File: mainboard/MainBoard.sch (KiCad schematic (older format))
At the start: 51 parts, among them J1 isoSPI, J11 Conn_01x02, J2 SWDebug, J3 IMD, J4 IO, U1 LTC6820, U10 REF2920, U2 HM2103, U3 M24M02, U4 M24M02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

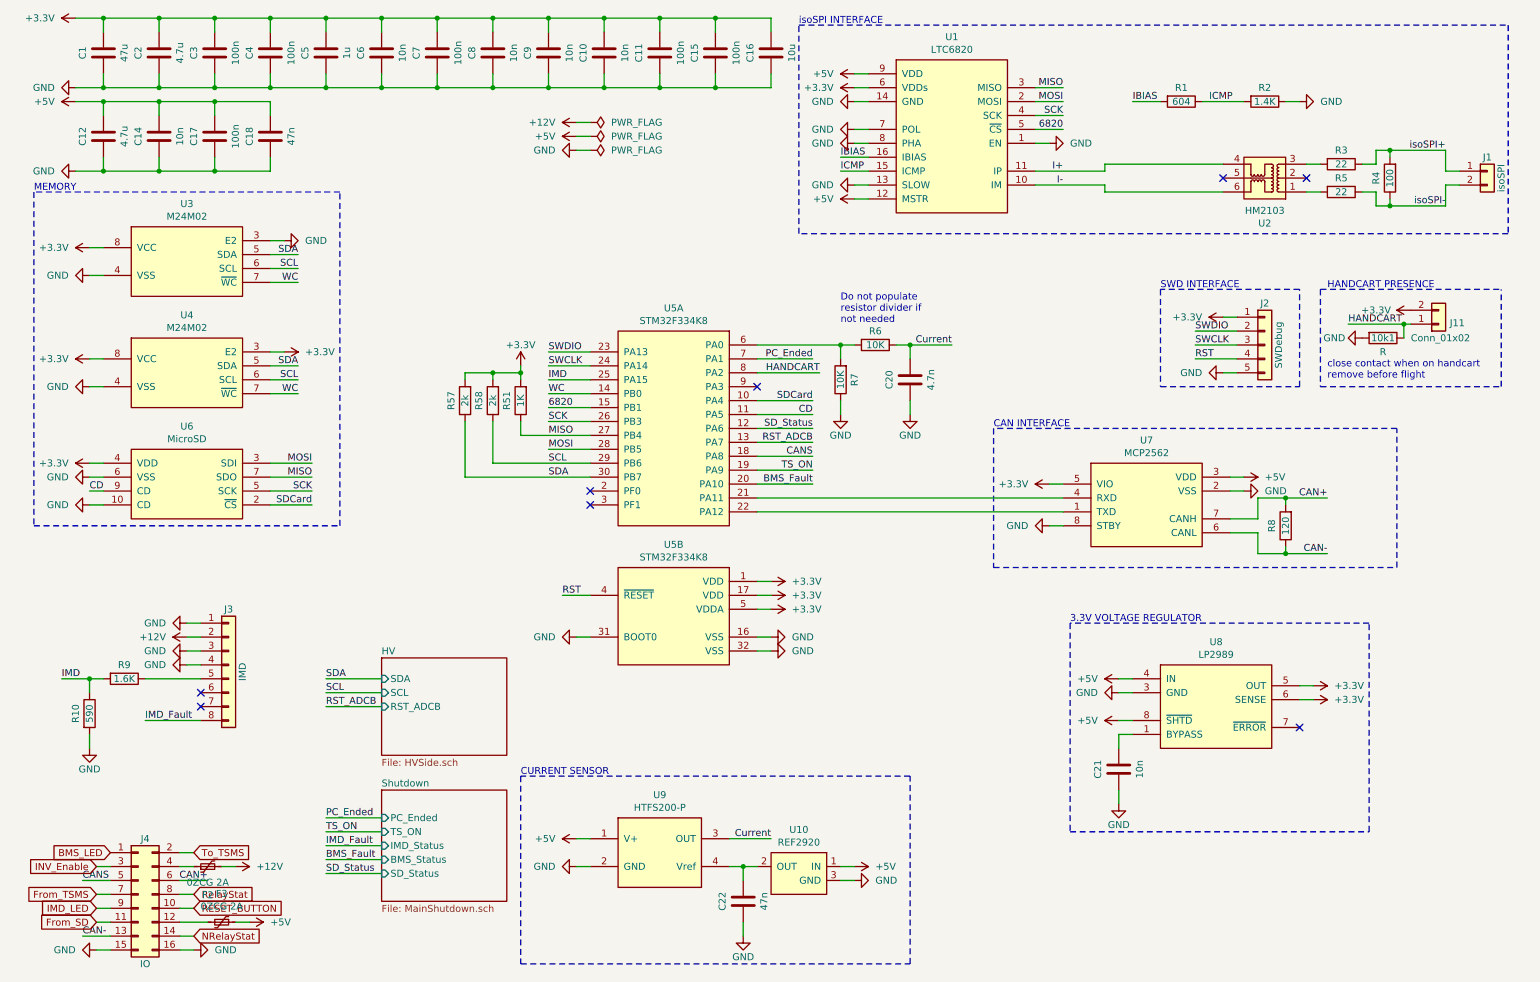
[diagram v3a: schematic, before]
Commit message: Shutdown logic to use gates, changed mosfets
Shutdown ported from new car, mosfets changed to higher VGS max
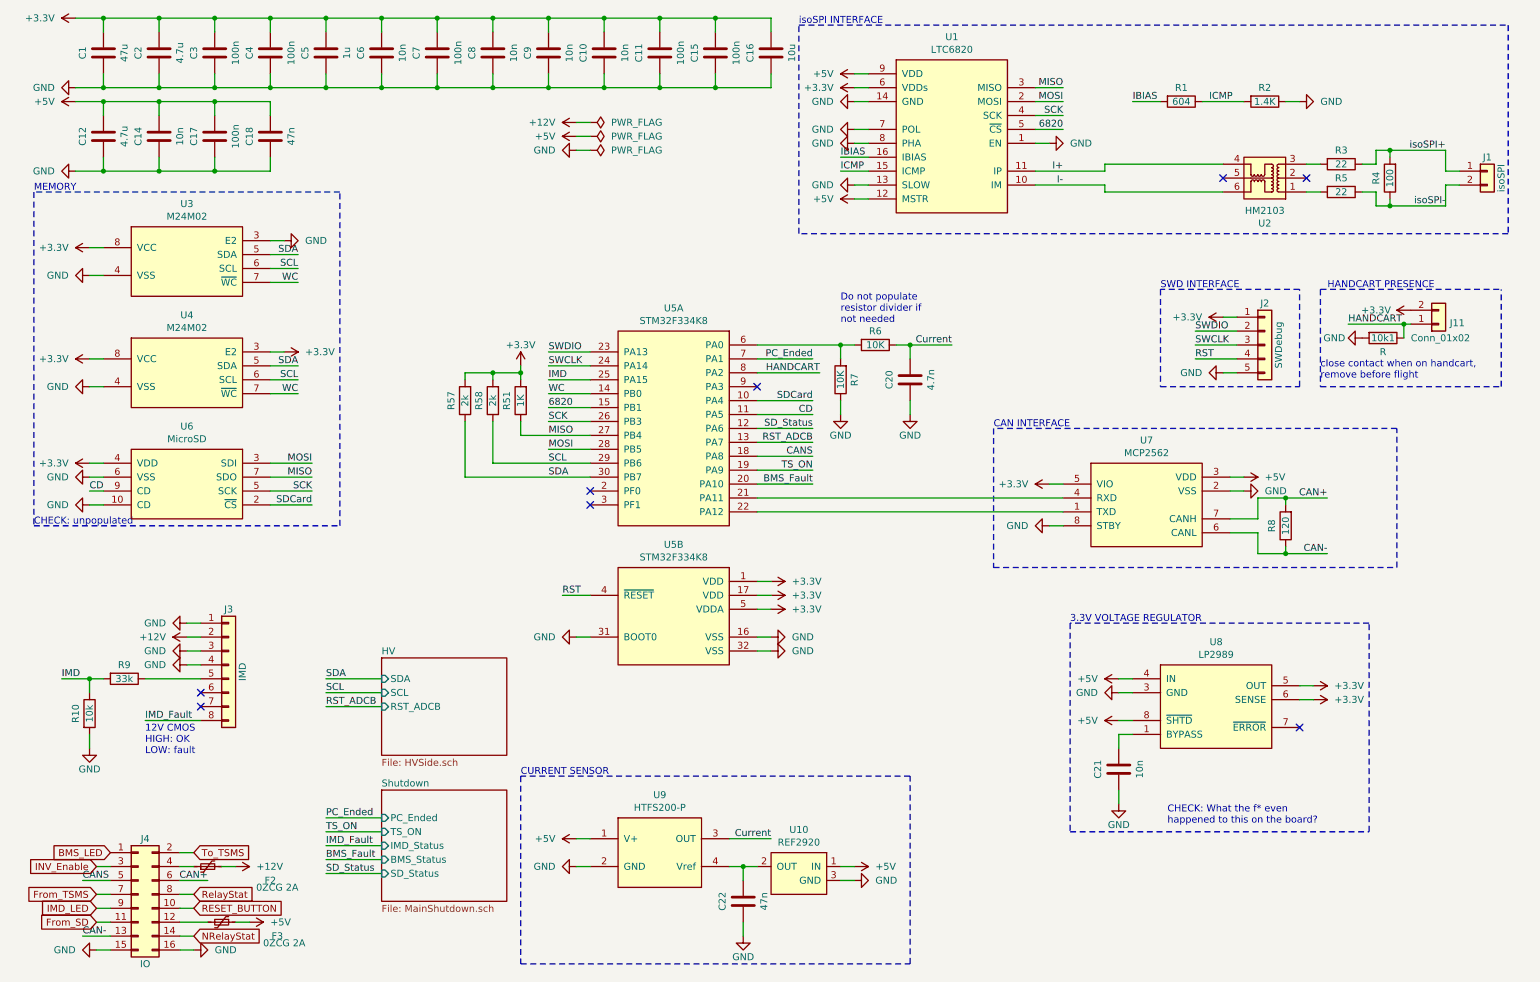
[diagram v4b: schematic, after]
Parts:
- R10: value 590 -> 10k
- R9: value 1.6K -> 33k
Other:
- note added: "12V CMOS\nHIGH: OK\nLOW: fault"
- note added: "CHECK: What the f* even \nhappened to this on the board?"
- note added: "CHECK: unpopulated"
- note added: "close contact when on handcart,\nremove before flight"
- note removed: "close contact when on handcart\nremove before flight"
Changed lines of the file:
@@
 Title ""
 Date ""
-Rev ""
+Rev "V3"
 Comp ""
 Comment1 ""
@@
 P 1000 5550
 F 0 "R10" V 900 5550 50  0000 C CNN
-F 1 "590" V 1000 5550 50  0000 C CNN
+F 1 "10k" V 1000 5550 50  0000 C CNN
 F 2 "Resistor_SMD:R_0805_2012Metric" V 930 5550 50  0001 C CNN
 F 3 "~" H 1000 5550 50  0001 C CNN
@@
 P 1250 5300
 F 0 "R9" V 1150 5300 50  0000 C CNN
-F 1 "1.6K" V 1250 5300 50  0000 C CNN
+F 1 "33k" V 1250 5300 50  0000 C CNN
 F 2 "Resistor_SMD:R_0805_2012Metric" V 1180 5300 50  0001 C CNN
 F 3 "~" H 1250 5300 50  0001 C CNN
@@
 U 1 1 5B2F3DA2
 P 1850 6650
-F 0 "F2" V 1645 6650 50  0000 C CNN
-F 1 "0ZCG 2A" V 1736 6650 50  0000 C CNN
+F 0 "F2" V 1750 6200 50  0000 C CNN
+F 1 "0ZCG 2A" V 1700 6150 50  0000 C CNN
 F 2 "Fuse:Fuse_1812_4532Metric" H 1900 6450 50  0001 L CNN
 F 3 "~" H 1850 6650 50  0001 C CNN
@@
 U 1 1 5B3092A1
 P 1950 7050
-F 0 "F3" V 1745 7050 50  0000 C CNN
-F 1 "0ZCG 2A" V 1836 7050 50  0000 C CNN
+F 0 "F3" V 2050 7450 50  0000 C CNN
+F 1 "0ZCG 2A" V 2100 7500 50  0000 C CNN
 F 2 "Fuse:Fuse_1812_4532Metric" H 2000 6850 50  0001 L CNN
 F 3 "~" H 1950 7050 50  0001 C CNN
@@
 Text Notes 9900 2500 0    50   ~ 0
 HANDCART PRESENCE
-Text Notes 9900 3150 0    50   ~ 0
-close contact when on handcart\nremove before flight
+Text Notes 9850 3150 0    50   ~ 0
+close contact when on handcart,\nremove before flight
 Wire Notes Line
 	9850 2500 9850 3200
@@
 	9850 3200 11150 3200
 NoConn ~ 5800 3200
+Text Notes 1400 5850 0    50   ~ 0
+12V CMOS\nHIGH: OK\nLOW: fault
+Text Notes 600  4200 0    50   ~ 0
+CHECK: unpopulated
+Text Notes 8750 6350 0    50   ~ 0
+CHECK: What the f* even \nhappened to this on the board?
 $EndSCHEMATC

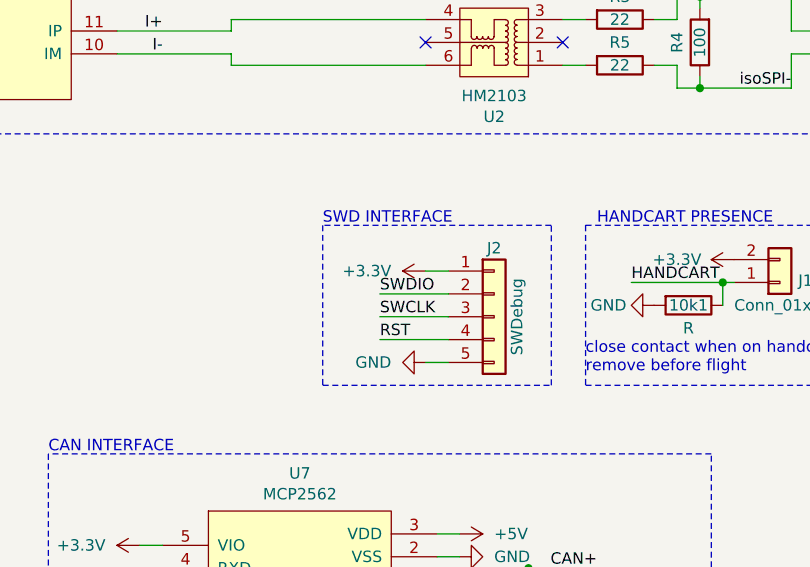
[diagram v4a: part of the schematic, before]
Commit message: new SWD connector
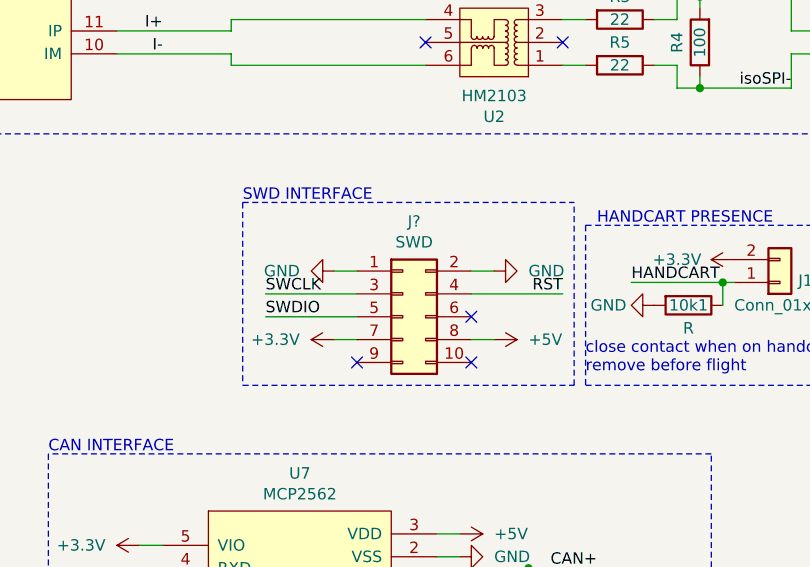
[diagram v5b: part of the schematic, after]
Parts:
- removed J2: SWDebug, Connector_PinHeader_2.54mm:PinHeader_1x05_P2.54mm_Vertical, symbol Connector_Generic:Conn_01x05
- added J?: SWD, symbol Connector_Generic:Conn_02x05_Odd_Even
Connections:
- net +3V3: now also J?.7 (Pin_7)
- net +5V: now also J?.8 (Pin_8)
- net GND: now also J?.1 (Pin_1), J?.2 (Pin_2)
- net RST: now also J?.4 (Pin_4)
- net SWCLK: now also J?.3 (Pin_3)
- net SWDIO: now also J?.5 (Pin_5)
- no-connect marks 8 -> 11
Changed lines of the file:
@@
 Text Label 4400 4700 0    50   ~ 0
 RST
-$Comp
-L Connector_Generic:Conn_01x05 J2
-U 1 1 5B04F48B
-P 9450 2900
-F 0 "J2" H 9450 3200 50  0000 C CNN
-F 1 "SWDebug" V 9550 2900 50  0000 C CNN
-F 2 "Connector_PinHeader_2.54mm:PinHeader_1x05_P2.54mm_Vertical" H 9450 2900 50  0001 C CNN
-F 3 "~" H 9450 2900 50  0001 C CNN
-	1    9450 2900
-	1    0    0    -1
-$EndComp
-Wire Wire Line
-	9250 2700 9150 2700
+Wire Wire Line
+	8850 3000 8750 3000
 $Comp
 L power:+3.3V #PWR021
 U 1 1 5B059441
-P 9150 2700
-F 0 "#PWR021" H 9150 2550 50  0001 C CNN
-F 1 "+3.3V" V 9150 2850 50  0000 L CNN
-F 2 "" H 9150 2700 50  0001 C CNN
-F 3 "" H 9150 2700 50  0001 C CNN
-	1    9150 2700
+P 8750 3000
+F 0 "#PWR021" H 8750 2850 50  0001 C CNN
+F 1 "+3.3V" V 8750 3150 50  0000 L CNN
+F 2 "" H 8750 3000 50  0001 C CNN
+F 3 "" H 8750 3000 50  0001 C CNN
+	1    8750 3000
 	0    -1   -1   0
 $EndComp
 Wire Wire Line
-	9250 3100 9150 3100
+	8850 2700 8750 2700
 $Comp
 L power:GND #PWR024
 U 1 1 5B0816C3
-P 9150 3100
-F 0 "#PWR024" H 9150 2850 50  0001 C CNN
-F 1 "GND" V 9150 2950 50  0000 R CNN
-F 2 "" H 9150 3100 50  0001 C CNN
-F 3 "" H 9150 3100 50  0001 C CNN
-	1    9150 3100
-	0    1    1    0
-$EndComp
-Text Label 8950 2800 0    50   ~ 0
+P 8750 2700
+F 0 "#PWR024" H 8750 2450 50  0001 C CNN
+F 1 "GND" V 8750 2550 50  0000 R CNN
+F 2 "" H 8750 2700 50  0001 C CNN
+F 3 "" H 8750 2700 50  0001 C CNN
+	1    8750 2700
+	0    1    1    0
+$EndComp
+Text Label 8450 2900 0    50   ~ 0
 SWDIO
-Text Label 8950 2900 0    50   ~ 0
+Text Label 8450 2800 0    50   ~ 0
 SWCLK
-Text Label 8950 3000 0    50   ~ 0
+Text Label 9750 2800 2    50   ~ 0
 RST
-Wire Wire Line
-	8950 2800 9250 2800
-Wire Wire Line
-	8950 2900 9250 2900
-Wire Wire Line
-	8950 3000 9250 3000
 Wire Notes Line
 	8050 4900 8050 6400
@@
 Wire Wire Line
 	4500 1500 4600 1500
-Wire Notes Line
-	9700 2500 8700 2500
-Wire Notes Line
-	8700 2500 8700 3200
-Wire Notes Line
-	8700 3200 9700 3200
-Wire Notes Line
-	9700 3200 9700 2500
-Text Notes 8700 2500 0    50   ~ 0
+Text Notes 8350 2400 0    50   ~ 0
 SWD INTERFACE
 $Comp
@@
 Text Notes 8750 6350 0    50   ~ 0
 CHECK: What the f* even \nhappened to this on the board?
+$Comp
+L Connector_Generic:Conn_02x05_Odd_Even J?
+U 1 1 606179E7
+P 9050 2900
+F 0 "J?" H 9100 3317 50  0000 C CNN
+F 1 "SWD" H 9100 3226 50  0000 C CNN
+F 2 "" H 9050 2900 50  0001 C CNN
+F 3 "~" H 9050 2900 50  0001 C CNN
+	1    9050 2900
+	1    0    0    -1
+$EndComp
+Wire Wire Line
+	8450 2800 8850 2800
+Wire Wire Line
+	8450 2900 8850 2900
+$Comp
+L power:+5V #PWR?
+U 1 1 6073E490
+P 9450 3000
+F 0 "#PWR?" H 9450 2850 50  0001 C CNN
+F 1 "+5V" V 9450 3150 50  0000 L CNN
+F 2 "" H 9450 3000 50  0001 C CNN
+F 3 "" H 9450 3000 50  0001 C CNN
+	1    9450 3000
+	0    1    -1   0
+$EndComp
+Wire Wire Line
+	9450 3000 9350 3000
+Wire Wire Line
+	9350 2800 9750 2800
+Wire Wire Line
+	9350 2700 9450 2700
+$Comp
+L power:GND #PWR?
+U 1 1 60784403
+P 9450 2700
+F 0 "#PWR?" H 9450 2450 50  0001 C CNN
+F 1 "GND" V 9450 2550 50  0000 R CNN
+F 2 "" H 9450 2700 50  0001 C CNN
+F 3 "" H 9450 2700 50  0001 C CNN
+	1    9450 2700
+	0    -1   -1   0
+$EndComp
+NoConn ~ 9350 2900
+NoConn ~ 9350 3100
+NoConn ~ 8850 3100
+Wire Notes Line
+	8350 3200 9800 3200
+Wire Notes Line
+	9800 3200 9800 2400
+Wire Notes Line
+	8350 2400 9800 2400
+Wire Notes Line
+	8350 2400 8350 3200
 $EndSCHEMATC

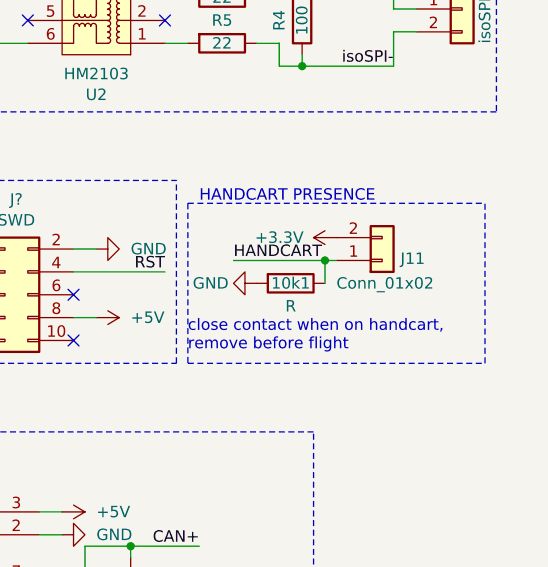
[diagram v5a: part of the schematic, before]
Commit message: renamed connector
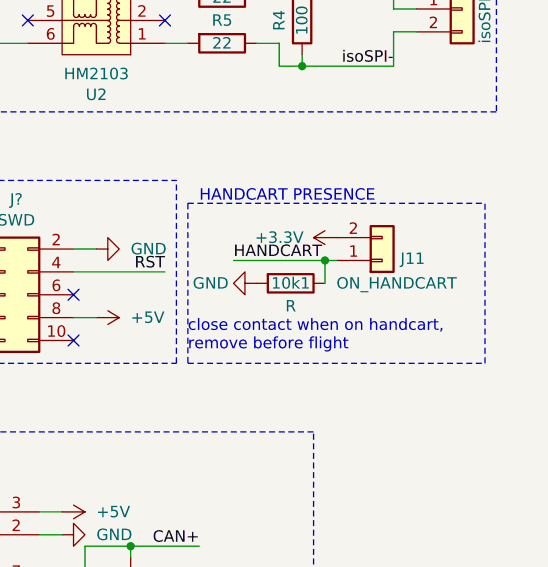
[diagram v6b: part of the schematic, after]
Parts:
- J11: value Conn_01x02 -> ON_HANDCART
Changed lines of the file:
@@
 P 10700 2750
 F 0 "J11" H 10780 2742 50  0000 L CNN
-F 1 "Conn_01x02" H 10500 2850 50  0000 L CNN
+F 1 "ON_HANDCART" H 10500 2850 50  0000 L CNN
 F 2 "" H 10700 2750 50  0001 C CNN
 F 3 "~" H 10700 2750 50  0001 C CNN
